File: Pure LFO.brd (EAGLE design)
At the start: 18.3 x 100 mm, 46 parts, among them T3 TRANS_PAIR, U1 DUAL_OPAMP, U2 QUAD_OPAMP

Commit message: LFO 2.1
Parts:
- removed L1, L2, L3: (no value), INSTRUO:LSG_T77K
- removed R16: 15K, rcl:R0805
- removed R18: 50K, rcl:R0805
- removed R19: 20K, rcl:R0805
- removed R20, R21, R22: 2K*, rcl:R0805
- removed U1: DUAL_OPAMP, INSTRUO:DUAL_OPAMP
- removed U2: QUAD_OPAMP, INSTRUO:QUAD_OPAMP
- added IC1: TL074, GMSN:SO14
- added IC2: TL072, GMSN:SO14
- added U$1, U$2: (no value), gmsnLogo:GMSN!_LOGO
- C1: value 47nF -> 5n1F; device rcl:C0805K -> GMSN:C0805
- C2, C3: value 10u -> 10uF; device rcl:153CLV-0505 -> GMSN:153CLV-0505
- C4, C5, C7, C8: value 0.1u -> 100nF; device rcl:C0805K -> GMSN:C0805
- C6: device rcl:C0805K -> GMSN:C0805
- D1, D2: value (none) -> STTH102A; device adafruit:SMADIODE -> GMSN:SMADIODE
- JP1: value M05X2SHD -> HEADER2X5SHD; device SparkFun-Connectors:2X5-SHROUDED -> GMSN:2X5-SHROUDED
- R1: value 1K -> 100R; device rcl:R0805 -> GMSN:R0805
- R10, R12, R14, R15, R17, R9: value 10K -> 10k; device rcl:R0805 -> GMSN:R0805
- R11: value 400R -> 402R; device rcl:R0805 -> GMSN:R0805
- R13, R8: value 2K -> 2k; device rcl:R0805 -> GMSN:R0805
- R2: value 300R? -> 3M3; device rcl:R0805 -> GMSN:R0805
- R3: value 3M -> 3k3; device rcl:R0805 -> GMSN:R0805
- R4: value 12K -> 12k; device rcl:R0805 -> GMSN:R0805
- R5: value 33K -> 33k; device rcl:R0805 -> GMSN:R0805
- R6: value 1K3 -> 1k3; device rcl:R0805 -> GMSN:R0805
- R7: value 3K3 -> 3k3; device rcl:R0805 -> GMSN:R0805
- RATE: value B100K -> B100k; device INSTRUO:Q-POT -> GMSN:POTENTIOMETER_9MM
- RATESW: value (none) -> SWITCH_TOGGLE_SPDT; device INSTRUO:TOGGLE_ON_OFF_ON -> GMSN:TOGGLE_SW
- SINE_OUT, SQU_OUT, TRI_OUT: value (none) -> SOCKET_MONO_3.5MMPJ301M-12; device INSTRUO:S_JACK -> GMSN:PJ301M-12
- T3: value TRANS_PAIR -> DMMT3904W-7-F; device QuBit:TRANS_PAIR -> GMSN:TRANS_PAIR
- TR1: value 100K -> 100k; device INSTRUO:TRIM_3269W -> GMSN:TRIMMER_TH
- TR2: device INSTRUO:TRIM_3269W -> GMSN:TRIMMER_TH
- moved R5 15.7 mm to (2.30, 49.9), flipped to the top
- moved C5 15.2 mm to (17.8, 61.6), flipped to the top
- moved C7 15.2 mm to (2.54, 81.9), flipped to the top
- moved R11 15.2 mm to (17.8, 80.6), flipped to the top
- moved R6 15.2 mm to (2.54, 59.1), flipped to the top
- moved R17 14.1 mm to (3.02, 68.1), flipped to the top, turned to 180 degrees
- moved R4 14.0 mm to (3.17, 55.2), flipped to the top
- moved R12 13.0 mm to (16.7, 102.9), flipped to the top
- moved R8 12.7 mm to (3.81, 102.9), flipped to the top
- moved R3 11.4 mm to (15.9, 87.0), flipped to the top
- moved R9 11.4 mm to (15.9, 84.7), flipped to the top
- moved D2 9.84 mm to (5.24, 37.6), flipped to the top
- moved TR1 9.84 mm to (5.24, 97.8), flipped to the top
- moved TR2 9.84 mm to (15.1, 97.8), flipped to the top
- moved D1 9.68 mm to (15.0, 37.6), flipped to the top
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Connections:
- removed net L_SIN: R21.2, SINE_OUT.NORM
- removed net L_SQU: R20.2, SQU_OUT.NORM
- removed net L_TRI: R22.2, TRI_OUT.NORM
- removed net N$13: L1.1, L1.4, L2.1, L2.4, L3.1, L3.4, R18.1, R5.1, RATE.P$3, U2.4OUT
- removed net N$15: L1.2, L1.3, R22.1
- removed net N$16: L2.2, L2.3, R21.1
- removed net N$17: L3.2, L3.3, R20.1
- removed net SINE: R17.1, SINE_OUT.TIP, U1.1OUT
- new net SINE_WAVE: IC1.10, IC2.1, R17.1
- new net SQUARE_WAVE: IC1.14, IC2.10, R5.1, RATE.P$3
- new net TRIANGLE_WAVE: C1.2, IC1.7, IC2.12, R4.2, R6.2
- net +12V: now also IC1.4, IC2.4; no longer U1.+VCC, U2.VCC++
- net -12V: now also IC1.11, IC2.11; no longer U1.-VCC, U2.VCC--
- net GND: now also IC1.13, IC1.5; no longer R16.1, R19.1, U2.2+IN, U2.4-IN
- net N$21: now also T3.5; no longer T3.E2
- net N$25: now also T3.1; no longer T3.B2
- net N$26: now also T3.4; no longer T3.E1
- net N$28: now also T3.2; no longer T3.B1
- net N$32: now also IC2.6, T3.6; no longer T3.C2, U1.-2IN
- net N$33: now also IC1.1, IC1.2; no longer U2.1-IN, U2.1OUT
- net N$34: now also IC2.5, T3.3; no longer T3.C1, U1.+2IN
- net N$35: now also IC1.3; no longer U2.1+IN
- net N$38: now also IC2.2; no longer R16.2, U1.-1IN
- net N$5: now also IC2.8, IC2.9, SQU_OUT.TIP; no longer R18.2, R19.2, U2.3+IN
- net N$6: now also IC1.6; no longer U2.2-IN
- net N$7: now also IC2.13, IC2.14; no longer C1.2, R4.2, R6.2, U2.2OUT
- net N$8: now also IC1.8, IC1.9, SINE_OUT.TIP; no longer SQU_OUT.TIP, U2.3-IN, U2.3OUT
- net N$9: now also IC1.12; no longer U2.4+IN
- net SINE_PRE: now also IC2.3, IC2.7; no longer U1.+1IN, U1.2OUT
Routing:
- net N$13: track 123.4 -> 0.00 mm, vias 1 -> 0
- net SQUARE_WAVE: track 0.00 -> 82.6 mm, vias 0 -> 1
- net N$8: track 33.7 -> 0.00 mm, vias 1 -> 0
- net N$7: track 15.9 -> 0.00 mm
- net N$17: track 9.26 -> 0.00 mm
- net N$5: track 8.84 -> 0.00 mm
- net N$15: track 7.94 -> 0.00 mm
- net SINE: track 7.54 -> 0.00 mm
- net -12V: track 95.0 -> 88.3 mm
- net N$25: track 25.9 -> 32.3 mm
- net SINE_PRE: track 11.8 -> 5.41 mm
- net N$16: track 6.28 -> 0.00 mm
- net +12V: track 90.1 -> 84.9 mm
- net N$6: track 63.1 -> 59.2 mm
- net L_SIN: track 3.92 -> 0.00 mm
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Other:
- board text added: "-12V"
- board text added: "Pure LFO V2.1"
- board text added: "copyright GMSN Ltd 2016"

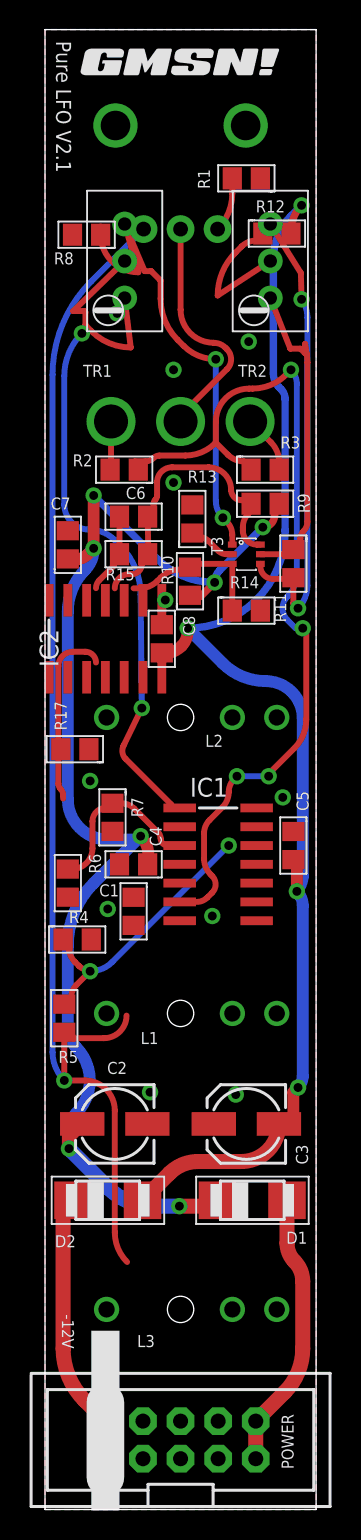
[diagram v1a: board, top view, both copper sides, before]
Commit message: LFO 2.2
LFO Updated to V2.2 20/4/21

Traces rerouted.
Schmitt Trigger error corrected.
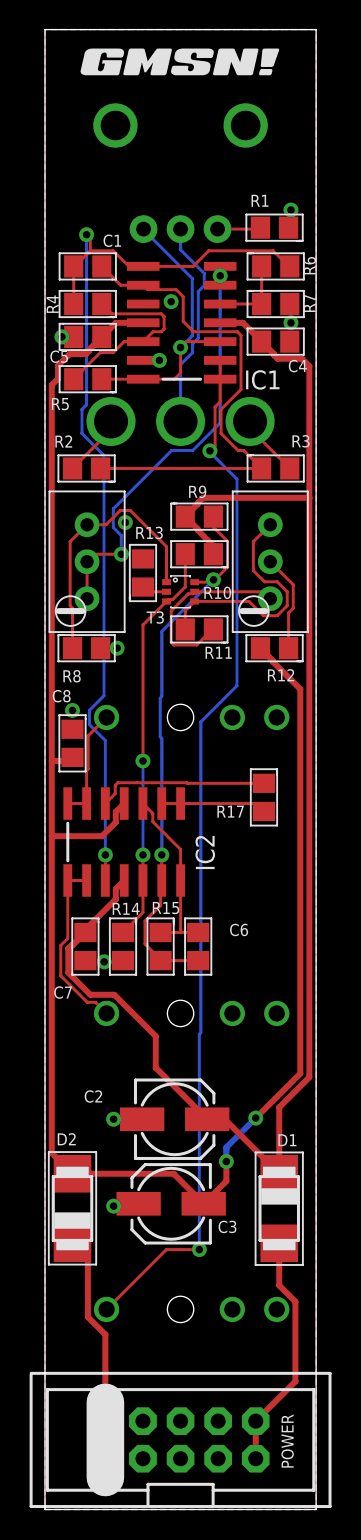
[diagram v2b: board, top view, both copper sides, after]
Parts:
- moved R6 44.0 mm to (16.6, 100.7), turned to 0 degrees
- moved C1 43.7 mm to (3.89, 100.7), turned to 180 degrees
- moved R5 43.2 mm to (3.89, 93.1), turned to 180 degrees
- moved R4 42.9 mm to (3.89, 98.2), turned to 180 degrees
- moved C5 37.1 mm to (3.89, 96.0), turned to 0 degrees
- moved IC1 36.7 mm to (10.2, 96.9), turned to 90 degrees
- moved C4 36.6 mm to (16.6, 95.6), turned to 0 degrees
- moved R7 36.4 mm to (16.6, 98.2), turned to 0 degrees
- moved C6 29.4 mm to (11.4, 54.8), turned to 90 degrees
- moved R12 28.0 mm to (16.5, 74.9), turned to 180 degrees
- moved R8 27.9 mm to (3.81, 74.9), turned to 0 degrees
- moved C7 27.2 mm to (3.73, 54.8), turned to 270 degrees
- moved R15 26.6 mm to (8.81, 54.8), turned to 270 degrees
- moved R14 24.2 mm to (6.27, 54.8), turned to 270 degrees
- moved TR1 20.5 mm to (2.70, 77.5)
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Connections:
- removed net N$38: IC2.2, R17.2
- new net N$10: IC2.8, IC2.9, R17.2
- net GND: now also IC1.10; no longer IC1.5
- net N$33: now also IC1.6, IC1.7; no longer IC1.1, IC1.2
- net N$35: now also IC1.5; no longer IC1.3
- net N$5: now also IC1.1, IC1.2; no longer IC2.8, IC2.9
- net N$6: now also IC1.9; no longer IC1.6
- net N$7: now also IC2.1, IC2.2; no longer IC2.13, IC2.14
- net N$8: now also IC2.13, IC2.14; no longer IC1.8, IC1.9
- net SINE_PRE: now also IC2.10; no longer IC2.3
- net SINE_WAVE: now also IC2.12; no longer IC1.10, IC2.1
- net SQUARE_WAVE: now also IC1.3; no longer IC2.10
- net TRIANGLE_WAVE: now also IC1.8, IC2.3; no longer IC1.7, IC2.12
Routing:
- net N$5: track 0.00 -> 70.2 mm, vias 0 -> 2
- net TRIANGLE_WAVE: track 0.48 -> 65.3 mm, vias 0 -> 2
- net SQUARE_WAVE: track 82.6 -> 19.8 mm
- net -12V: track 88.3 -> 121.2 mm, vias 4 -> 2
- net N$6: track 59.2 -> 34.1 mm, vias 4 -> 0
- net N$33: track 50.2 -> 29.2 mm
- net +12V: track 84.9 -> 103.9 mm, vias 7 -> 0
- net N$34: track 10.3 -> 27.5 mm, vias 0 -> 2
- net N$32: track 20.0 -> 37.2 mm, vias 0 -> 2
- net N$26: track 31.7 -> 16.5 mm, vias 2 -> 0
- net N$25: track 32.3 -> 18.1 mm, vias 2 -> 0
- net N$38: track 12.4 -> 0.00 mm
- net N$7: track 0.00 -> 12.1 mm
- net SINE_WAVE: track 0.00 -> 11.6 mm
- net N$21: track 22.1 -> 12.9 mm
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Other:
- board text added: "Pure LFO V2.2 cc-by 4.0 2021 The Little Red Hen"
- board text removed: "-12V"
- board text removed: "L1"
- board text removed: "L2"
- board text removed: "L3"
- board text removed: "Pure LFO V2.1"
- board text removed: "TR1"
- board text removed: "TR2"
- board text removed: "copyright GMSN Ltd 2016"
